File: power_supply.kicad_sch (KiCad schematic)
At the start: 62 parts, among them Q1201 2N7002, Q1202 DMP2120U, U1201 TL431PK, U1202 TL431PK, U1203 TL431PK, U1204 MCP1825T-330, U1205 NCV8164ASN120T1G, U1206 MCP1825T-330, U1207 NCV8164ASN250T1G, U1208 NCV8164ASN330T1G

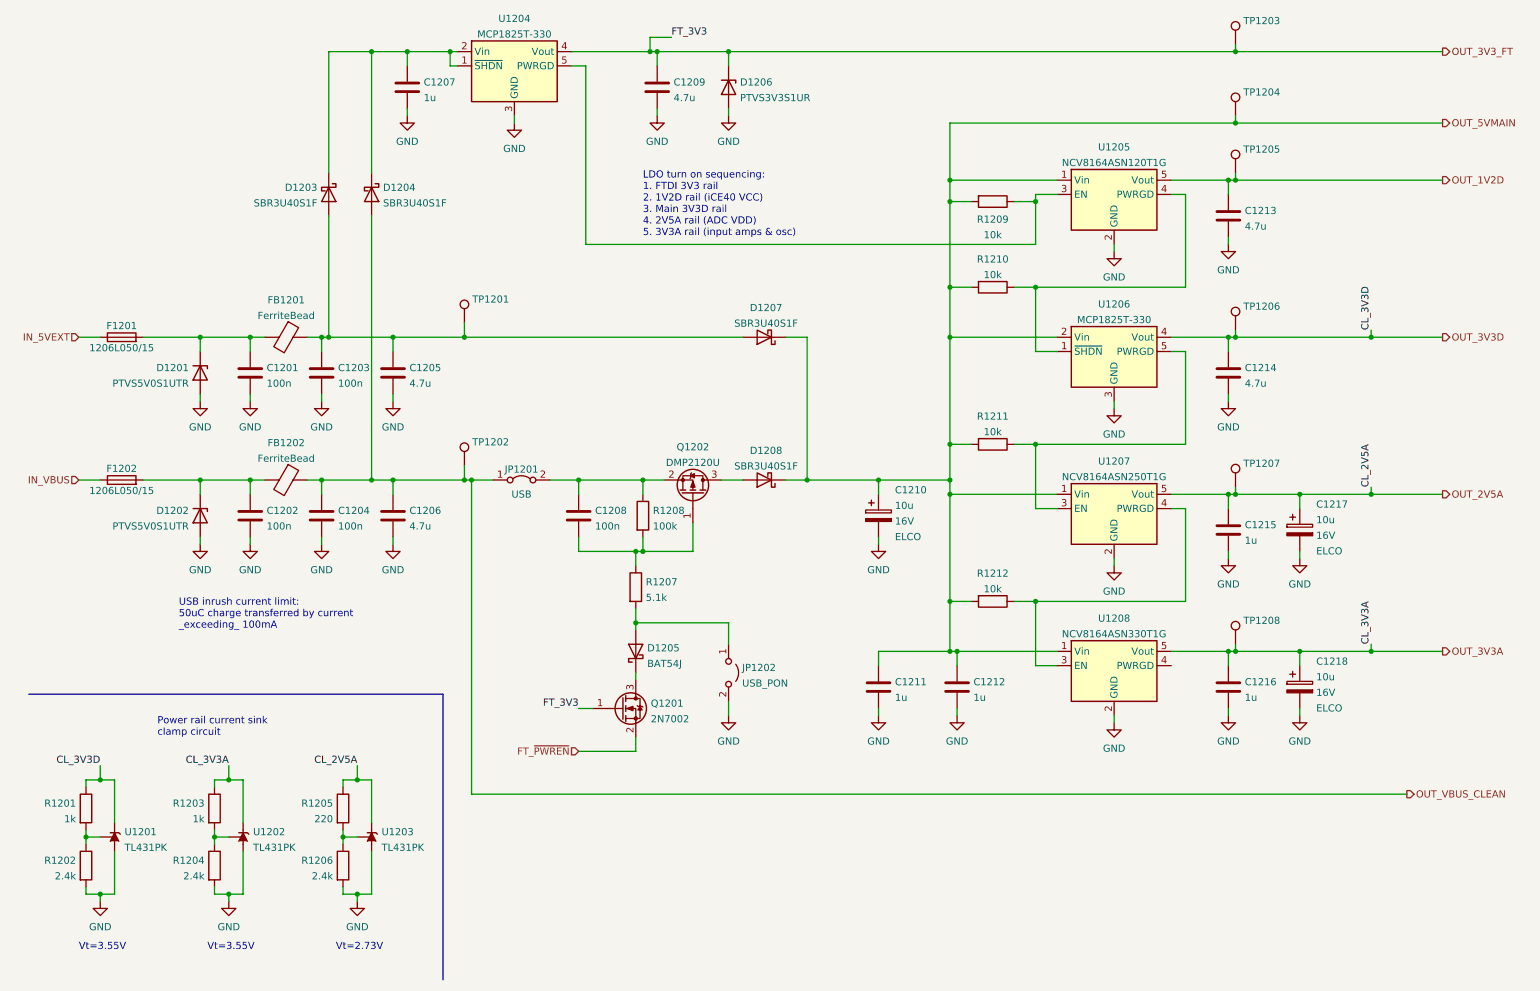
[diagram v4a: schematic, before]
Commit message: Schematic: better LDO output capacitor selection, clarified BOM
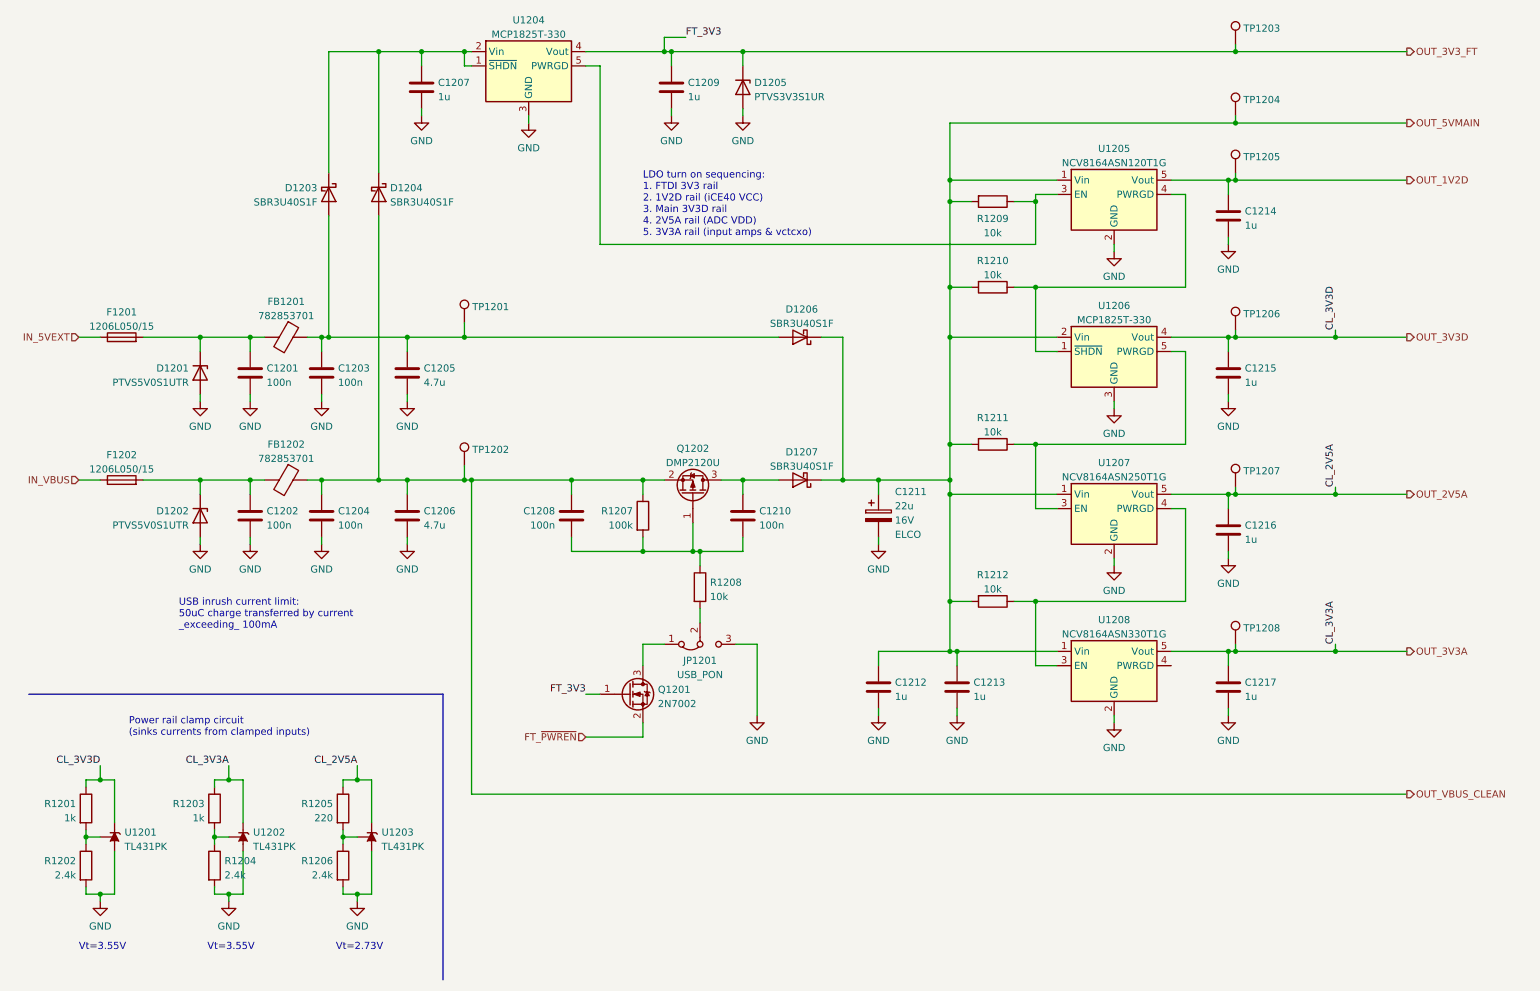
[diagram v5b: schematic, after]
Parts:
- removed C1215: 1u, Capacitor_SMD:C_0805_2012Metric, symbol Device:C
- removed C1217, C1218: 10u, Capacitor_SMD:CP_Elec_4x5.8, symbol Device:C_Polarized
- removed D1205: BAT54J, Diode_SMD:D_SOD-323F, symbol Diode:BAT54J
- removed JP1201: USB, Connector_PinHeader_2.54mm:PinHeader_1x02_P2.54mm_Vertical, symbol Jumper:Jumper_2_Bridged
- removed JP1202: USB_PON, Connector_PinHeader_2.54mm:PinHeader_1x02_P2.54mm_Vertical, symbol Jumper:Jumper_2_Open
- added C1208: 100n, Capacitor_SMD:C_0805_2012Metric, symbol Device:C
- added C1217: 1u, Capacitor_SMD:C_0805_2012Metric, symbol Device:C
- added JP1201: USB_PON, Connector_PinHeader_2.54mm:PinHeader_1x03_P2.54mm_Vertical, symbol Jumper:Jumper_3_Bridged12
- C1201, C1202, C1203, C1204, C1205, C1206, C1207, C1216: Spec1 16V -> (none); Spec2 X5R -> (none); Tolerance 20% -> (none)
- C1209: value 4.7u -> 1u; Spec1 16V -> (none); Spec2 X5R -> (none); Tolerance 20% -> (none)
- C1210: renamed from C1208; Spec1 16V -> (none); Spec2 X5R -> (none); Tolerance 20% -> (none)
- C1211: renamed from C1210; value 10u -> 22u; footprint Capacitor_SMD:CP_Elec_4x5.8 -> Capacitor_SMD:CP_Elec_5x5.7
- C1212: renamed from C1211; Spec1 16V -> (none); Spec2 X5R -> (none); Tolerance 20% -> (none)
- C1213: renamed from C1212; Spec1 16V -> (none); Spec2 X5R -> (none); Tolerance 20% -> (none)
- C1214: renamed from C1213; value 4.7u -> 1u; Spec1 16V -> (none); Spec2 X5R -> (none); Tolerance 20% -> (none)
- C1215: renamed from C1214; value 4.7u -> 1u; Spec1 16V -> (none); Spec2 X5R -> (none); Tolerance 20% -> (none)
- FB1201, FB1202: value FerriteBead -> 782853701; footprint (none) -> Inductor_SMD:L_0805_2012Metric_Pad1.05x1.20mm_HandSolder
- R1208: renamed from R1207; value 5.1k -> 10k
- renumbered D1206 to D1205, D1207 to D1206, D1208 to D1207, R1208 to R1207
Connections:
- net GND: now also C1217.2, JP1201.3 (B)
- net OUT_2V5A: now also C1216.1
- net OUT_3V3A: now also C1217.1; no longer C1216.1
- net OUT_VBUS_CLEAN: now also Q1202.2 (S), R1207.1, C1208.1
- net at R1208.2: now also JP1201.2 (C)
- net at C1210.2, Q1202.1 (G), R1207.2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: now also C1208.2
- net at D1207.2 (A), Q1202.3 (D): now also C1210.1
- net at Q1201.3 (D): now also JP1201.1 (A)
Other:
- note added: "LDO turn on sequencing: 1. FTDI 3V3 rail 2. 1V2D rail (iCE40 VCC) 3. Main 3V3D rail 4. 2V5A rail (ADC VDD) 5. 3V3A rail (input amps & vctcxo)"
- note added: "Power rail clamp circuit (sinks currents from clamped inputs)"
- note removed: "LDO turn on sequencing: 1. FTDI 3V3 rail 2. 1V2D rail (iCE40 VCC) 3. Main 3V3D rail 4. 2V5A rail (ADC VDD) 5. 3V3A rail (input amps & osc)"
- note removed: "Power rail current sink clamp circuit"
- moved on the sheet: C1205, C1206, C1207, C1209, C1210, D1204, D1205, D1206, D1207, Q1201, R1208, U1204

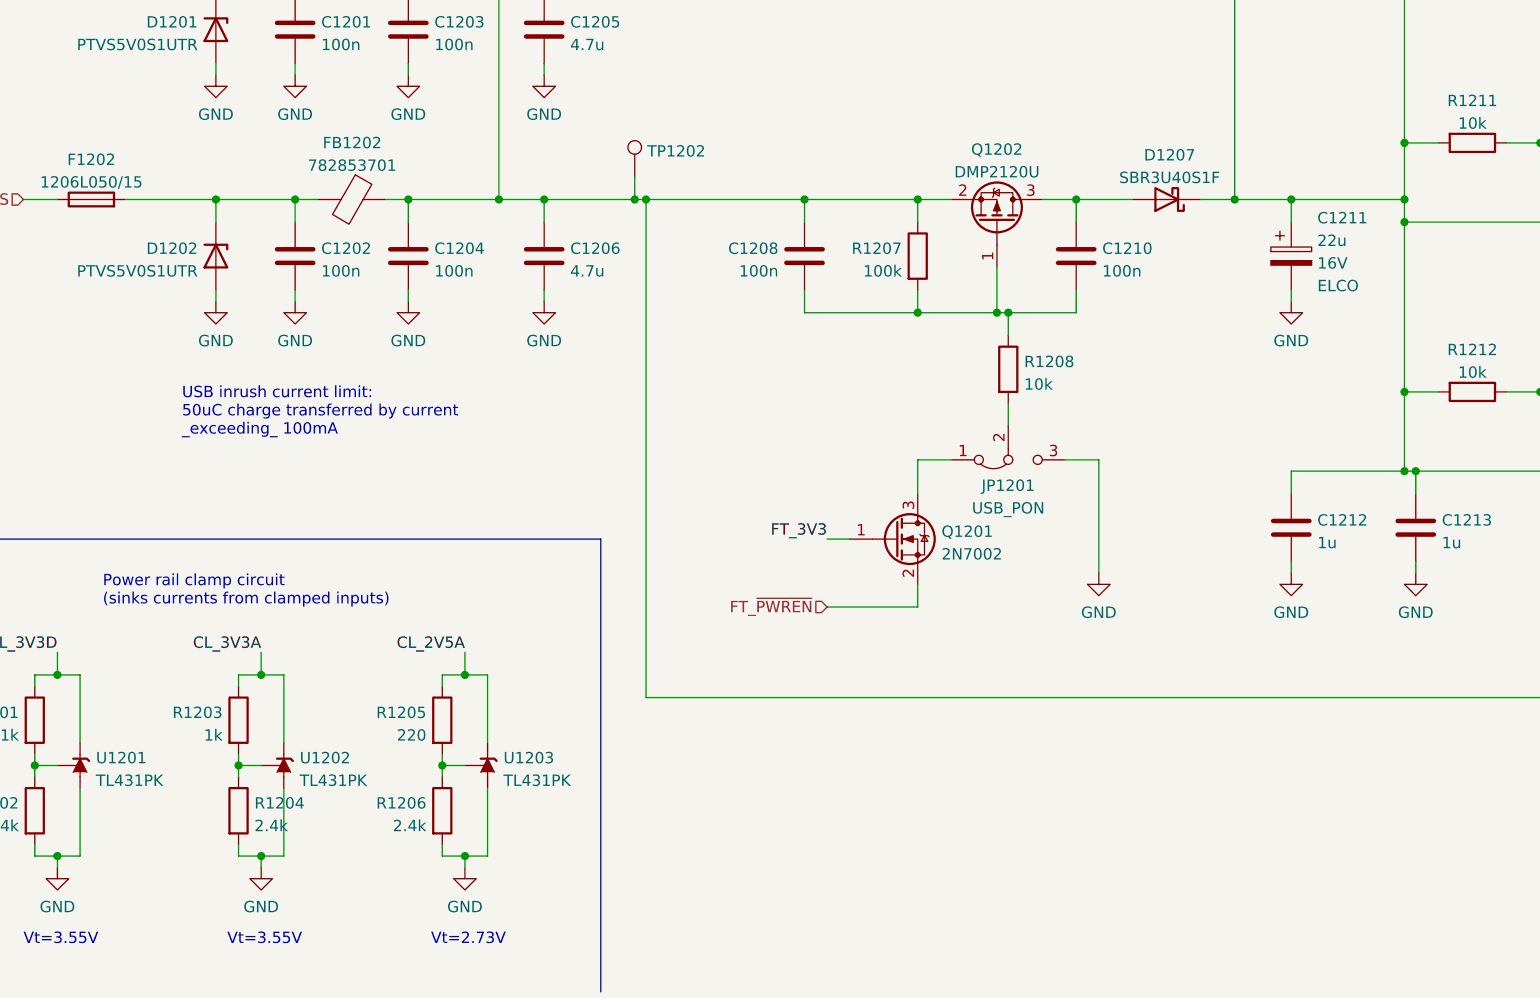
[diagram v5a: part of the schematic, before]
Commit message: Schematic: yet another update -Improve way caps are specified once again -Update cap voltages based on ESD simulation -Make anti-aliasing LC filter more practical - with much less inductors -Specify Mfr & MfrPN for almost all components (most from Mouser, some from Digikey)
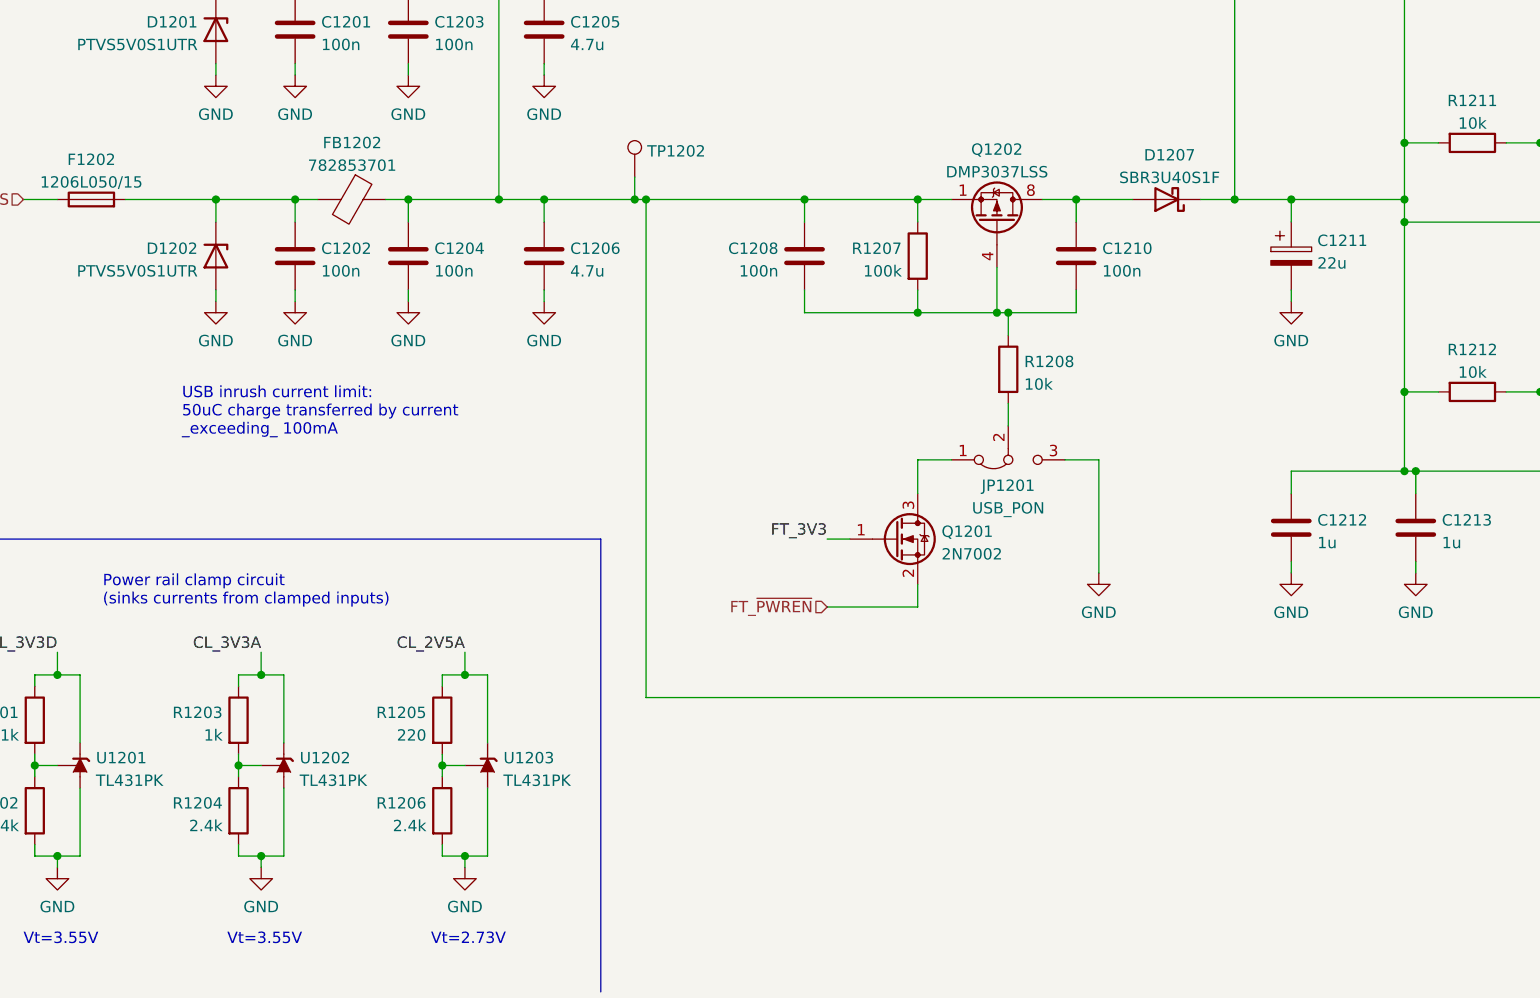
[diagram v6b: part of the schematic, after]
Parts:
- removed Q1202: DMP2120U, Package_TO_SOT_SMD:SOT-23, symbol Device:Q_PMOS_GSD
- added Q1202: DMP3037LSS, Package_SO:SOIC-8_3.9x4.9mm_P1.27mm, symbol Transistor_FET:FDS9435A
- C1201, C1202, C1203, C1204, C1208, C1210: Mfr (none) -> Samsung; Mfr PN (none) -> CL21B104KBFNNNE
- C1205, C1206: Mfr (none) -> Murata; Mfr PN (none) -> GRM21BR71C475ME51
- C1207, C1209, C1212, C1213, C1214, C1215, C1216, C1217: Mfr (none) -> Samsung; Mfr PN (none) -> CL21B105KOFNNNG
- C1211: footprint Capacitor_SMD:CP_Elec_5x5.7 -> Capacitor_SMD:CP_Elec_4x5.8; Mfr (none) -> Nichicon; Mfr PN (none) -> UCL1C220MCL6GS; Spec1 16V -> (none); Spec2 ELCO -> (none); Tolerance 20% -> (none)
- D1201, D1202: footprint (none) -> Diode_SMD:D_SOD-123; Mfr (none) -> Nexperia; Mfr PN (none) -> PTVS5V0S1UTR,115
- D1203, D1204, D1206, D1207: footprint (none) -> Diode_SMD:D_SOD-123; Mfr (none) -> DIODES; Mfr PN (none) -> SBR3U40S1FQ-7
- D1205: footprint (none) -> Diode_SMD:D_SOD-123; Mfr (none) -> Nexperia; Mfr PN (none) -> PTVS3V3S1UR,115
- F1201, F1202: Mfr (none) -> Littelfuse; Mfr PN (none) -> 1206L050/15
- FB1201, FB1202: Mfr (none) -> Wurth; Mfr PN (none) -> 782853701
- Q1201: Mfr (none) -> Nexperia; Mfr PN (none) -> 2N7002NXAKR
- R1201, R1202, R1203, R1204, R1205, R1206, R1207, R1208, R1209, R1210, R1211, R1212: Tolerance 5% -> (none)
- U1201, U1202, U1203: Mfr (none) -> Texas Instruments; Mfr PN (none) -> TL431ACPK
- U1204, U1206: Mfr (none) -> Microchip; Mfr PN (none) -> MCP1825T-3302E/DC
- U1205: Mfr (none) -> onsemi; Mfr PN (none) -> NCV8164ASN120T1G
- U1207: Mfr (none) -> onsemi; Mfr PN (none) -> NCV8164ASN250T1G
- U1208: Mfr (none) -> onsemi; Mfr PN (none) -> NCV8164ASN330T1G
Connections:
- net OUT_VBUS_CLEAN: now also Q1202.1 (S), Q1202.2 (S), Q1202.3 (S)
- net at C1210.1, D1207.2 (A): now also Q1202.5 (D), Q1202.6 (D), Q1202.7 (D), Q1202.8 (D)
- net at C1208.2, C1210.2, R1207.2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: now also Q1202.4 (G)
